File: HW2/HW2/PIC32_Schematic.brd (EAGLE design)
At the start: 50 x 50 mm, 22 parts

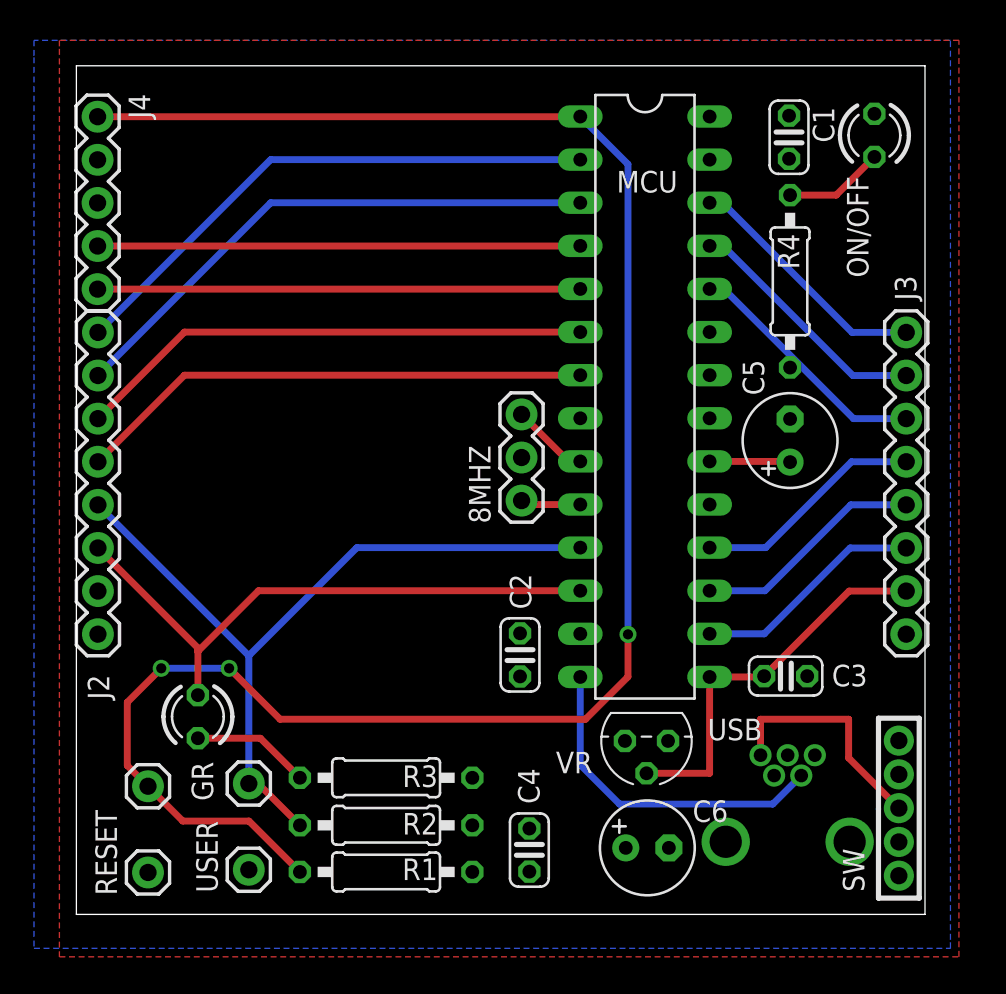
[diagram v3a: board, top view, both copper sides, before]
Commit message: All connections are wired
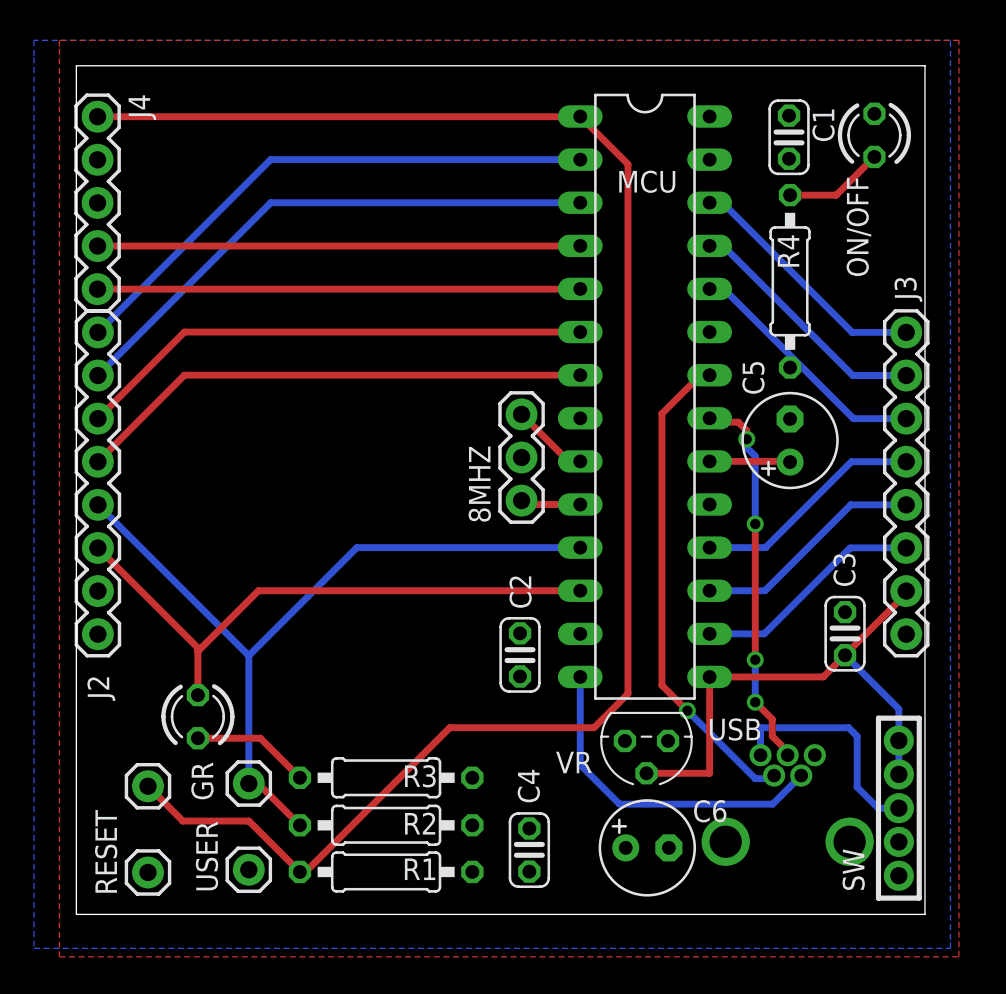
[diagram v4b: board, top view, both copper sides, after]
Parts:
- moved C3 4.30 mm to (45.3, 16.5), turned to 90 degrees
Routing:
- net D-: track 0.00 -> 28.7 mm, vias 0 -> 1
- net D+: track 0.00 -> 22.7 mm, vias 0 -> 4
- net MCLR: track 111.7 -> 98.3 mm, vias 3 -> 0
- net +5V: track 23.1 -> 31.7 mm
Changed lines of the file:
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@@
 <setting verticaltext="up"/>
 </settings>
-<grid distance="0.5" unitdist="mm" unit="mm" style="lines" multiple="1" display="yes" altdistance="0.25" altunitdist="mm" altunit="mm"/>
+<grid distance="0.5" unitdist="mm" unit="mm" style="lines" multiple="1" display="yes" altdistance="0.125" altunitdist="mm" altunit="mm"/>
 <layers>
 <layer number="1" name="Top" color="4" fill="1" visible="yes" active="yes"/>
@@
 <attribute name="VALUE" x="23.473" y="17.068" size="1.27" layer="27" ratio="10" rot="R270"/>
 </element>
-<element name="C3" library="ME433" package="C025-024X044" value="0.1uF" x="41.79" y="14.04" smashed="yes">
-<attribute name="NAME" x="44.512" y="13.437" size="1.27" layer="25" ratio="10"/>
-<attribute name="VALUE" x="40.012" y="15.873" size="1.27" layer="27" ratio="10"/>
+<element name="C3" library="ME433" package="C025-024X044" value="0.1uF" x="45.29" y="16.54" smashed="yes" rot="R90">
+<attribute name="NAME" x="45.893" y="19.262" size="1.27" layer="25" ratio="10" rot="R90"/>
+<attribute name="VALUE" x="43.457" y="14.762" size="1.27" layer="27" ratio="10" rot="R90"/>
 </element>
 <element name="C4" library="ME433" package="C025-024X044" value="0.1uF" x="26.69" y="3.79" smashed="yes" rot="R90">
@@
 <contactref element="USB" pad="D-"/>
 <contactref element="MCU" pad="22"/>
-<wire x1="41.11" y1="8.18" x2="37.31" y2="31.77" width="0" layer="19" extent="1-1"/>
+<wire x1="36.5" y1="31.5" x2="37" y2="31.5" width="0.4064" layer="1"/>
+<wire x1="34.5" y1="29.5" x2="36.5" y2="31.5" width="0.4064" layer="1"/>
+<wire x1="34.5" y1="13.5" x2="34.5" y2="29.5" width="0.4064" layer="1"/>
+<wire x1="36" y1="12" x2="34.5" y2="13.5" width="0.4064" layer="1"/>
+<wire x1="40" y1="8" x2="36" y2="12" width="0.4064" layer="16"/>
+<wire x1="41" y1="8" x2="40" y2="8" width="0.4064" layer="16"/>
+<wire x1="37" y1="31.5" x2="37.31" y2="31.77" width="0.4064" layer="1"/>
+<wire x1="41" y1="8" x2="41.11" y2="8.18" width="0.4064" layer="16"/>
+<via x="36" y="12" extent="1-16" drill="0.6"/>
 </signal>
 <signal name="D+">
 <contactref element="MCU" pad="21"/>
 <contactref element="USB" pad="D+"/>
-<wire x1="41.91" y1="9.38" x2="37.31" y2="29.23" width="0" layer="19" extent="1-1"/>
+<wire x1="39" y1="29" x2="37.5" y2="29" width="0.4064" layer="1"/>
+<wire x1="39.5" y1="28.5" x2="39" y2="29" width="0.4064" layer="1"/>
+<wire x1="39.5" y1="28" x2="39.5" y2="28.5" width="0.4064" layer="1"/>
+<wire x1="39.5" y1="27.5" x2="39.5" y2="28" width="0.4064" layer="16"/>
+<wire x1="40" y1="27" x2="39.5" y2="27.5" width="0.4064" layer="16"/>
+<wire x1="40" y1="23" x2="40" y2="27" width="0.4064" layer="16"/>
+<wire x1="40" y1="15" x2="40" y2="23" width="0.4064" layer="1"/>
+<wire x1="40" y1="12.5" x2="40" y2="15" width="0.4064" layer="16"/>
+<wire x1="41" y1="11.5" x2="40" y2="12.5" width="0.4064" layer="1"/>
+<wire x1="41" y1="10.5" x2="41" y2="11.5" width="0.4064" layer="1"/>
+<wire x1="42" y1="9.5" x2="41" y2="10.5" width="0.4064" layer="1"/>
+<wire x1="37.5" y1="29" x2="37.31" y2="29.23" width="0.4064" layer="1"/>
+<wire x1="42" y1="9.5" x2="41.91" y2="9.38" width="0.4064" layer="1"/>
+<via x="39.5" y="28" extent="1-16" drill="0.6"/>
+<via x="40" y="23" extent="1-16" drill="0.6"/>
+<via x="40" y="15" extent="1-16" drill="0.6"/>
+<via x="40" y="12.5" extent="1-16" drill="0.6"/>
 </signal>
 <signal name="N$9">
@@
 <contactref element="VR" pad="2"/>
 <contactref element="C3" pad="1"/>
-<wire x1="40.52" y1="14.04" x2="45.53" y2="19.05" width="0.4064" layer="1"/>
-<wire x1="45.53" y1="19.05" x2="48.895" y2="19.05" width="0.4064" layer="1"/>
-<wire x1="37.31" y1="13.99" x2="40.47" y2="13.99" width="0.4064" layer="1"/>
-<wire x1="40.47" y1="13.99" x2="40.52" y2="14.04" width="0.4064" layer="1"/>
 <wire x1="37.31" y1="13.99" x2="37.31" y2="8.315" width="0.4064" layer="1"/>
 <wire x1="37.31" y1="8.315" x2="33.59" y2="8.315" width="0.4064" layer="1"/>
-<wire x1="40.52" y1="14.04" x2="48.46" y2="8.25" width="0" layer="19" extent="1-1"/>
+<wire x1="37.31" y1="13.99" x2="44.01" y2="13.99" width="0.4064" layer="1"/>
+<wire x1="44.01" y1="13.99" x2="45.29" y2="15.27" width="0.4064" layer="1"/>
+<wire x1="48.46" y1="8.25" x2="48.46" y2="12.1" width="0.4064" layer="16"/>
+<wire x1="48.46" y1="12.1" x2="45.29" y2="15.27" width="0.4064" layer="16"/>
+<wire x1="48.5" y1="18.5" x2="48.5" y2="19" width="0.4064" layer="1"/>
+<wire x1="45.5" y1="15.5" x2="48.5" y2="18.5" width="0.4064" layer="1"/>
+<wire x1="48.5" y1="19" x2="48.895" y2="19.05" width="0.4064" layer="1"/>
+<wire x1="45.5" y1="15.5" x2="45.29" y2="15.27" width="0.4064" layer="1"/>
 </signal>
 <signal name="A3">
@@
 <wire x1="10.17" y1="5.5" x2="6.27" y2="5.5" width="0.4064" layer="1"/>
 <wire x1="6.27" y1="5.5" x2="4.22" y2="7.55" width="0.4064" layer="1"/>
-<wire x1="4.22" y1="7.55" x2="3" y2="8.77" width="0.4064" layer="1"/>
-<wire x1="3" y1="8.77" x2="3" y2="12.5" width="0.4064" layer="1"/>
-<wire x1="3" y1="12.5" x2="5" y2="14.5" width="0.4064" layer="1"/>
-<via x="5" y="14.5" extent="1-16" drill="0.6"/>
-<wire x1="5" y1="14.5" x2="9" y2="14.5" width="0.4064" layer="16"/>
-<via x="9" y="14.5" extent="1-16" drill="0.6"/>
-<wire x1="9" y1="14.5" x2="12" y2="11.5" width="0.4064" layer="1"/>
-<wire x1="12" y1="11.5" x2="30" y2="11.5" width="0.4064" layer="1"/>
-<wire x1="30" y1="11.5" x2="32.5" y2="14" width="0.4064" layer="1"/>
-<wire x1="32.5" y1="14" x2="32.5" y2="16.5" width="0.4064" layer="1"/>
-<via x="32.5" y="16.5" extent="1-16" drill="0.6"/>
-<wire x1="32.5" y1="16.5" x2="32.5" y2="44.2" width="0.4064" layer="16"/>
-<wire x1="32.5" y1="44.2" x2="29.69" y2="47.01" width="0.4064" layer="16"/>
+<wire x1="13.5" y1="2.5" x2="22" y2="11" width="0.4064" layer="1"/>
+<wire x1="13.5" y1="2.5" x2="13.17" y2="2.5" width="0.4064" layer="1"/>
+<wire x1="22" y1="11" x2="30.5" y2="11" width="0.4064" layer="1"/>
+<wire x1="30.5" y1="11" x2="32.5" y2="13" width="0.4064" layer="1"/>
+<wire x1="32.5" y1="13" x2="32.5" y2="44.2" width="0.4064" layer="1"/>
+<wire x1="32.5" y1="44.2" x2="29.69" y2="47.01" width="0.4064" layer="1"/>
 </signal>
 <signal name="+3V3">
@@
 <contactref element="SW" pad="3"/>
 <contactref element="USB" pad="VBUS"/>
-<wire x1="40.31" y1="9.38" x2="40.31" y2="11.5" width="0.4064" layer="1"/>
-<wire x1="40.31" y1="11.5" x2="45.5" y2="11.5" width="0.4064" layer="1"/>
-<wire x1="45.5" y1="11.5" x2="45.5" y2="9.22" width="0.4064" layer="1"/>
-<wire x1="45.5" y1="9.22" x2="48.46" y2="6.26" width="0.4064" layer="1"/>
+<wire x1="40.31" y1="9.38" x2="40.31" y2="11" width="0.4064" layer="16"/>
+<wire x1="40.31" y1="11" x2="45.5" y2="11" width="0.4064" layer="16"/>
+<wire x1="45.5" y1="11" x2="46" y2="10.5" width="0.4064" layer="16"/>
+<wire x1="46" y1="10.5" x2="46" y2="7.5" width="0.4064" layer="16"/>
+<wire x1="46" y1="7.5" x2="47.24" y2="6.26" width="0.4064" layer="16"/>
+<wire x1="47.24" y1="6.26" x2="48.46" y2="6.26" width="0.4064" layer="16"/>
 </signal>
 <signal name="B7">

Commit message: Board is complete; on to error checking
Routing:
- net A4: track 35.1 -> 36.6 mm
- net MCLR: track 98.3 -> 99.1 mm
- net D+: track 22.7 -> 23.4 mm, vias 4 -> 3
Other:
- board text added: "+3.3V"
- board text added: "+5V"
- board text added: "2016"
- board text added: "A0"
- board text added: "A1"
- board text added: "A4"
- board text added: "Alexey"
- board text added: "B13"
- board text added: "B14"
- board text added: "B15"
- board text added: "B2"
- board text added: "B3"
- board text added: "B4"
- board text added: "B7"
- board text added: "B8"
- board text added: "B9"
- board text added: "GND"
- board text added: "ME 433"
- board text added: "Revinski"
- board text added: "^"

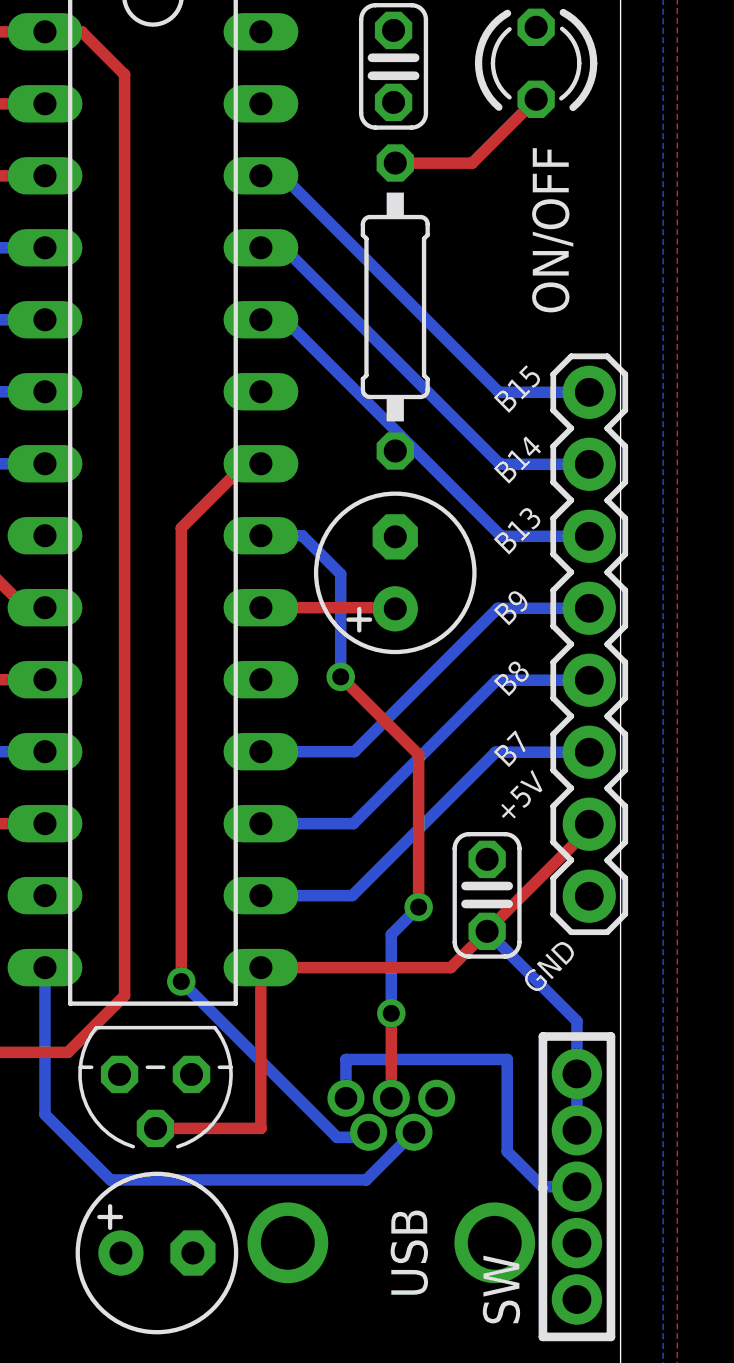
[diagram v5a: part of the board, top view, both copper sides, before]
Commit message: Error check complete.
6 errors I can't figure out.... Drill size errors for vie holes (even
though everything is fine) and two overlap errors that I fixed, but they
somehow persist...
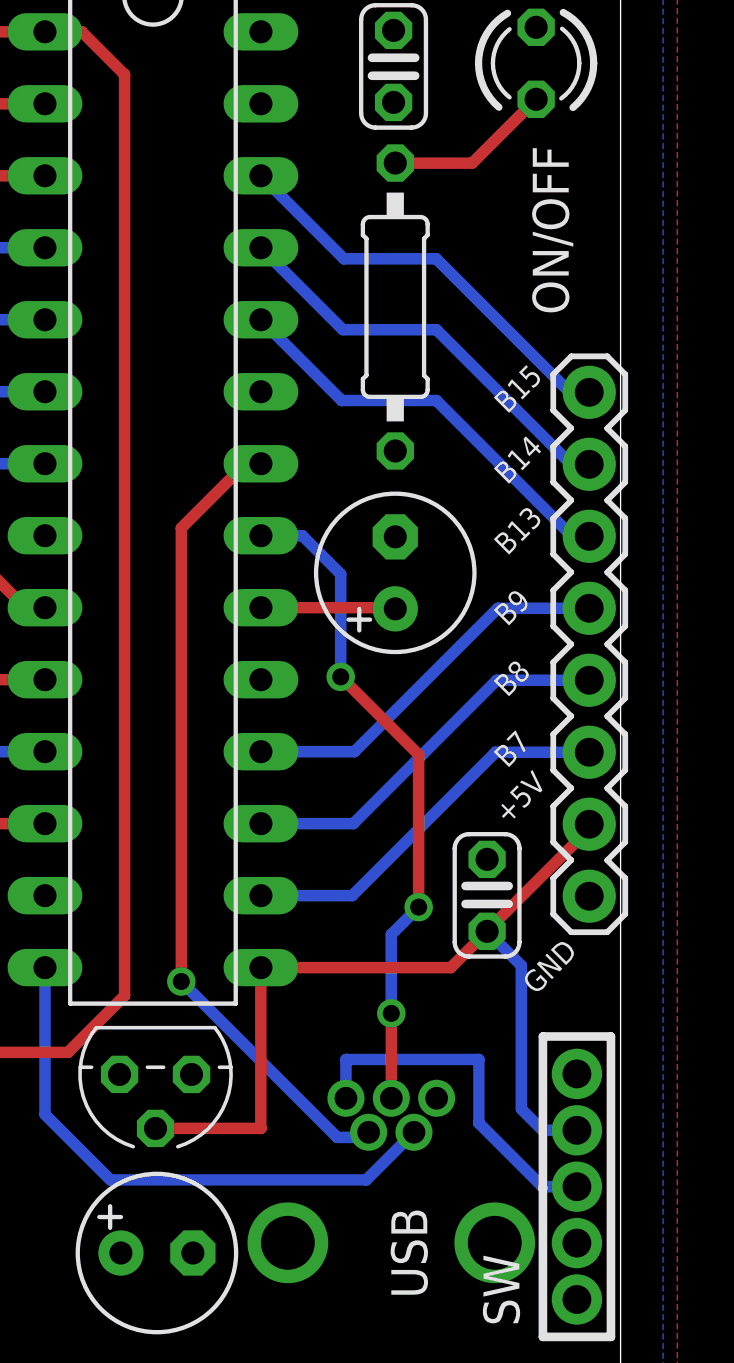
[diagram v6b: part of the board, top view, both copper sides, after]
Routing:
- net +5V: track 31.7 -> 32.4 mm
- net VBUS: track 13.3 -> 12.7 mm
